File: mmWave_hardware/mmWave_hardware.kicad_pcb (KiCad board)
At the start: 6 copper layers, 49 x 21.6 mm, 48 parts, among them J1 Conn_02x08_Top_Bottom, U1 IWRL6432BDBAAMFR, U2 W25Q128JVS, U3 AMS1117-3.3, U4 TPS628502QDRLRQ1, Y1 40.000

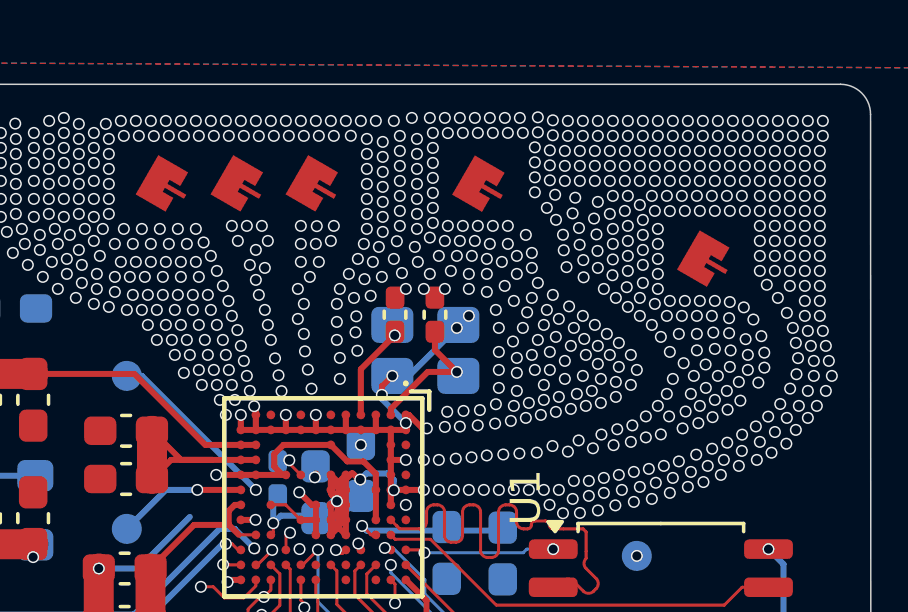
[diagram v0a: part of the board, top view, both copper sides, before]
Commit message: unrouting started
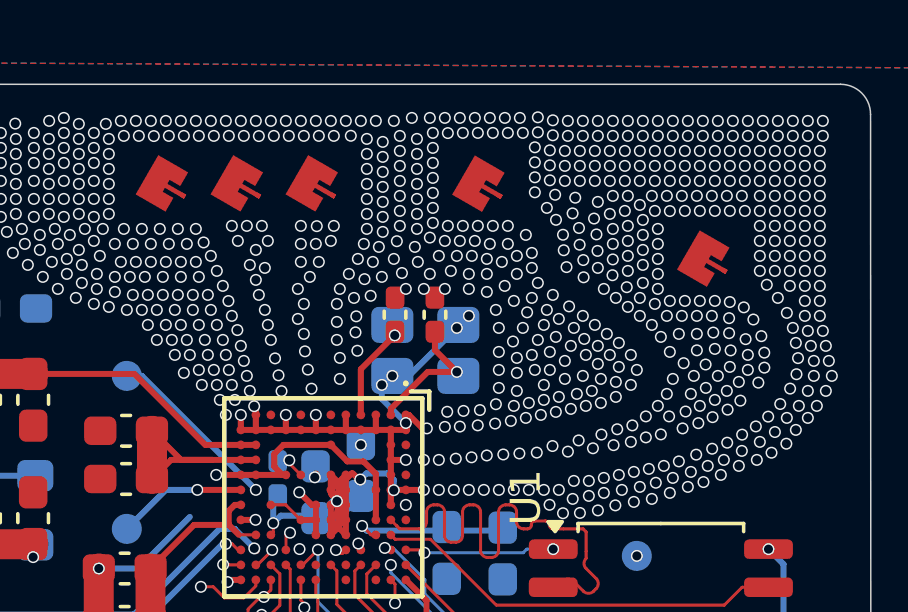
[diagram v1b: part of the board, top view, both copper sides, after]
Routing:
- net UART_RTS: track 42.3 -> 0.88 mm
- net GPIO_5: track 41.8 -> 0.69 mm
- net 1v8: track 78.6 -> 70.7 mm

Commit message: unrouted all
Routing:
- net GND: track 75.7 -> 0.00 mm
- net 1v8: track 70.7 -> 0.00 mm
- net 3v3: track 66.2 -> 0.00 mm
- net RS232_TX: track 52.1 -> 0.00 mm
- net SPI0_CLK: track 51.7 -> 0.00 mm
- net RS232_RX: track 51.0 -> 0.00 mm
- net SPI0_CS0_N: track 48.9 -> 0.00 mm
- net SPI0_MISO: track 45.0 -> 0.00 mm
- net SPI0_MOSI: track 44.9 -> 0.00 mm
- net UART_RX: track 40.4 -> 0.00 mm
- net GPIO_2: track 39.0 -> 0.00 mm
- net UART_TX: track 36.8 -> 0.00 mm
- net NRST_MAIN: track 35.4 -> 0.00 mm
- net VIN: track 23.0 -> 0.00 mm
- net /QSPI_1: track 17.1 -> 0.00 mm
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
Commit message: routing done
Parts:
- moved R3 10.2 mm to (58.5, 61.6)
- moved R6 9.69 mm to (58.5, 64.0)
- moved R2 7.50 mm to (58.5, 62.8)
- moved R4 7.22 mm to (57.9, 71.4)
- moved TP5 6.23 mm to (73.1, 69.3)
- moved C20 6.22 mm to (58.0, 67.2), turned to 90 degrees
- moved R5 5.37 mm to (57.9, 73.1)
- moved TP4 1.82 mm to (73.2, 66.4)
- moved R7 1.00 mm to (60.6, 67.5)
- moved C21 0.88 mm to (62.1, 70.7), turned to -90 degrees
- moved C18 0.43 mm to (64.6, 72.8)
- moved C9 0.14 mm to (76.5, 73.5)
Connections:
- J1 pad 10: SPI0_CS0_N -> UART_RTS
- J1 pad 11: SPI0_MISO -> UART_RX
- J1 pad 12: SPI0_MOSI -> UART_TX
- J1 pad 13: RS232_TX -> SPI0_CS0_N
- J1 pad 14: RS232_RX -> SPI0_CLK
- J1 pad 15: NRST_MAIN -> SPI0_MOSI
- J1 pad 16: VIN -> SPI0_MISO
- J1 pad 2: GPIO_2 -> VIN
- J1 pad 3: GND -> GPIO_2
- J1 pad 5: GND -> RS232_RX
- J1 pad 6: UART_RTS -> RS232_TX
- J1 pad 7: UART_RX -> unconnected-(J1-Pin_7-Pad7)
- J1 pad 8: UART_TX -> NRST_MAIN
- J1 pad 9: SPI0_CLK -> unconnected-(J1-Pin_9-Pad9)
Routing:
- net 3v3: track 0.00 -> 80.6 mm
- net GND: track 0.00 -> 52.3 mm
- net SPI0_CS0_N: track 0.00 -> 42.8 mm
- net 1v8: track 0.00 -> 42.5 mm, vias 6 -> 5
- net RS232_RX: track 0.00 -> 38.9 mm
- net SPI0_CLK: track 0.00 -> 38.0 mm
- net VIN: track 0.00 -> 35.1 mm, vias 3 -> 1
- net RS232_TX: track 0.00 -> 35.0 mm, vias 2 -> 1
- net SPI0_MOSI: track 0.00 -> 33.7 mm
- net SPI0_MISO: track 0.00 -> 33.7 mm
- net GPIO_2: track 0.00 -> 31.7 mm
- net UART_RX: track 0.00 -> 30.3 mm
- net UART_TX: track 0.00 -> 30.1 mm
- net NRST_MAIN: track 0.00 -> 29.6 mm
- net GPIO_5: track 0.00 -> 29.1 mm
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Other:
- board text removed: "ABCS"
- board text removed: "If you can see this, You have voided your warranty"

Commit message: Final PCB(Probably)
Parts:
- moved C10 78.1 mm to (144.8, 109.8)
- moved C11 78.1 mm to (141.4, 107.4)
- moved C12 78.1 mm to (141.4, 109.2)
- moved C13 78.1 mm to (136.7, 105.7)
- moved C14 78.1 mm to (138.3, 105.7)
- moved C17 78.1 mm to (149.2, 104.1)
- moved C18 78.1 mm to (132.9, 110.7)
- moved C19 78.1 mm to (129.6, 99.5)
- moved C2 78.1 mm to (151.7, 99.0)
- moved C20 78.1 mm to (126.3, 105.1)
- moved C21 78.1 mm to (130.3, 108.5)
- moved C22 78.1 mm to (136.3, 105.2)
- moved C23 78.1 mm to (137.6, 98.7)
- moved C24 78.1 mm to (133.9, 101.7)
- moved C3 78.1 mm to (152.1, 106.9)
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
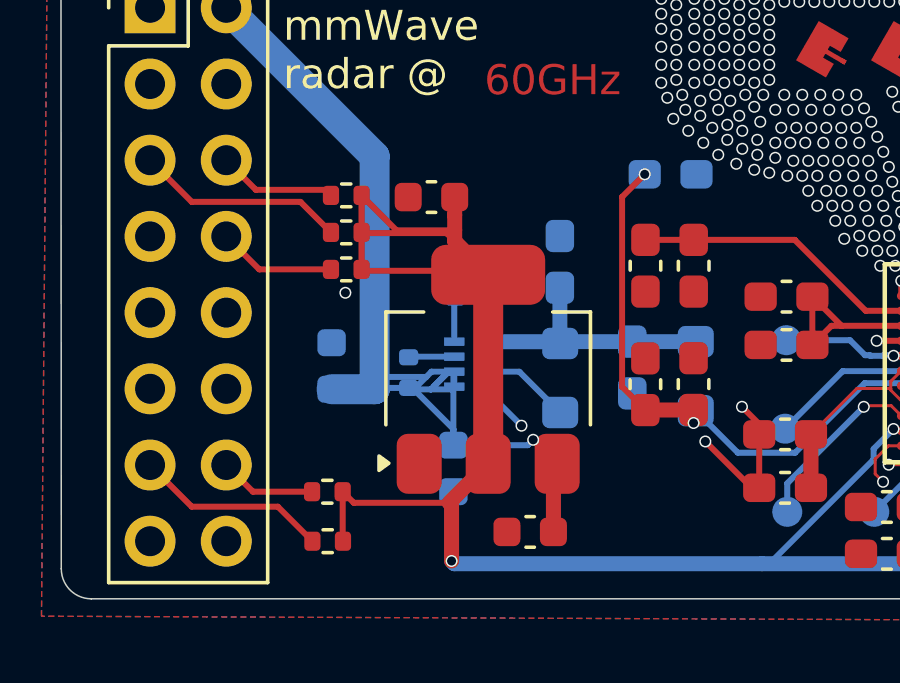
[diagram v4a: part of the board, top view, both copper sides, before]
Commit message: fixed footprint issue
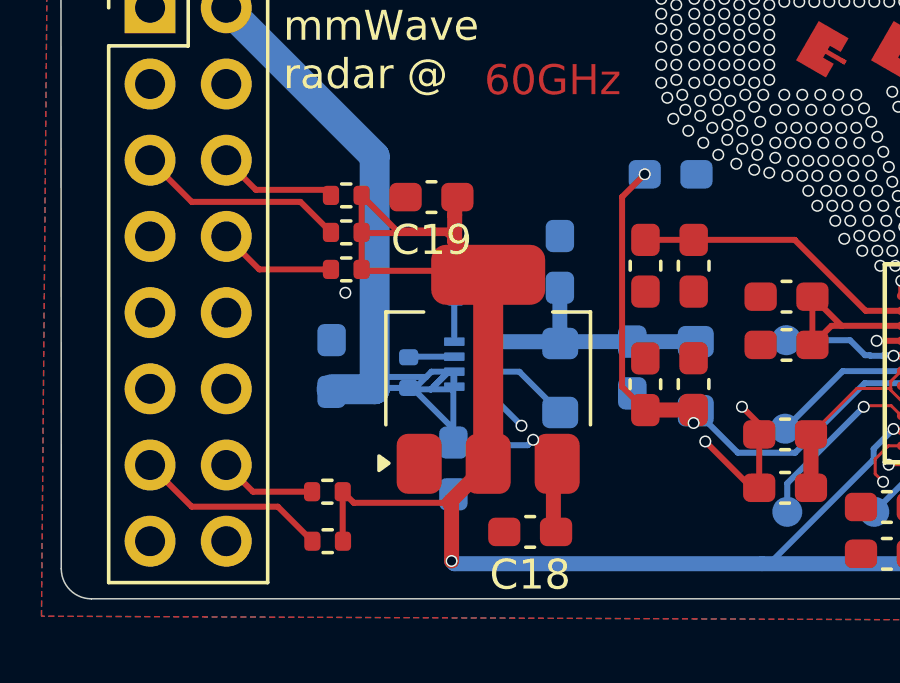
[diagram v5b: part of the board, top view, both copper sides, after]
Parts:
- C18, C19, C20, C21: footprint Capacitor_SMD:C_0603_1608Metric -> Capacitor_SMD:C_0603_1608Metric_Pad1.08x0.95mm_HandSolder

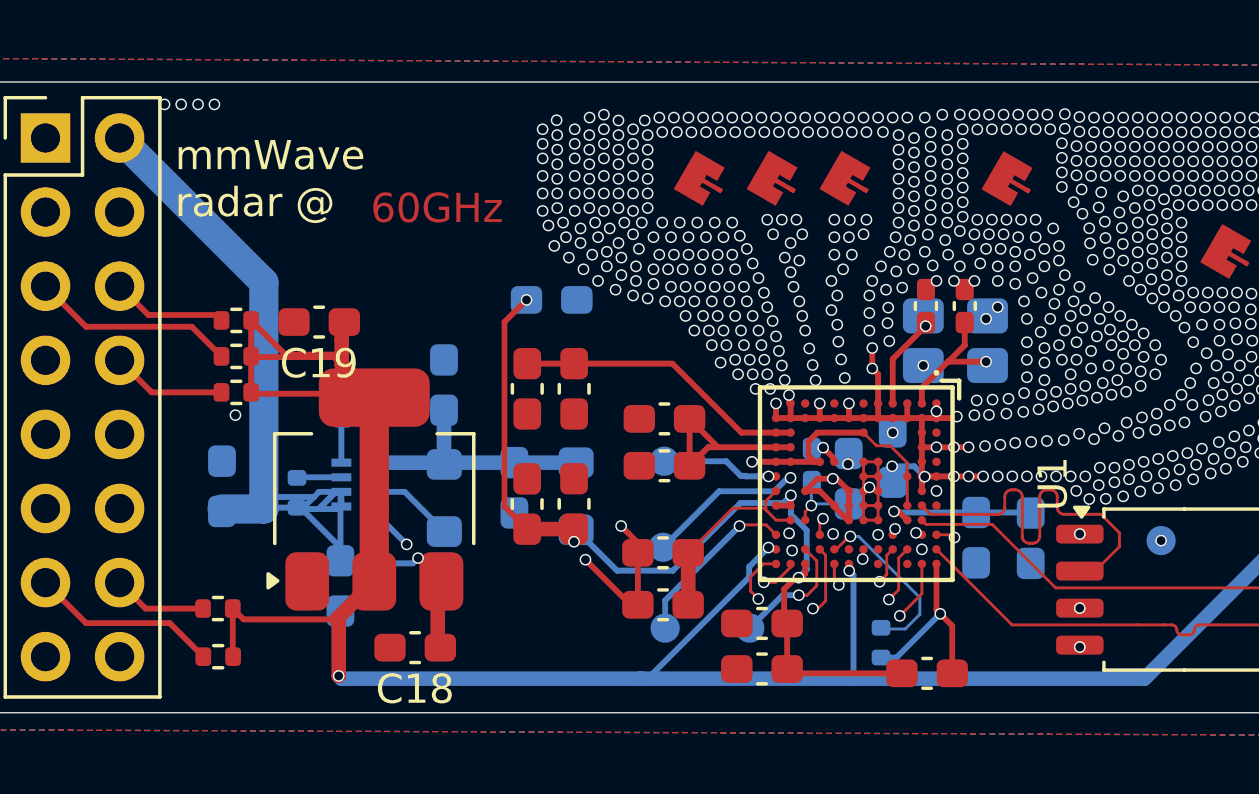
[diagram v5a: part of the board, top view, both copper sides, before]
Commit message: changed silkscreen
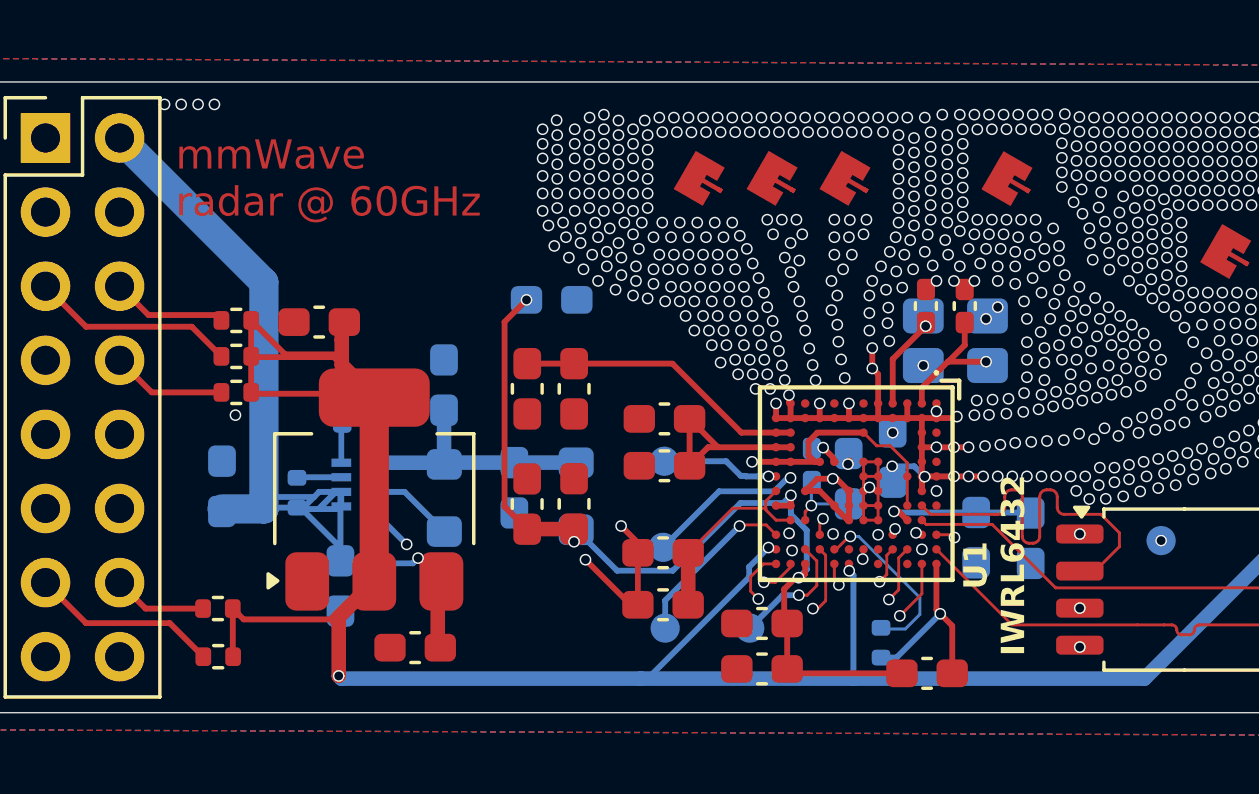
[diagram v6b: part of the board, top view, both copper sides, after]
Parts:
- R8: footprint Resistor_SMD:R_0402_1005Metric -> Resistor_SMD:R_0402_1005Metric_Pad0.72x0.64mm_HandSolder
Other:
- board text added: "U1 IWRL6432"
- board text added: "mmWave radar @ 60GHz"
- board text removed: "60GHz"
- board text removed: "mmWave radar @"
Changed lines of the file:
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@@
 		(at 147.997655 105.041 -90)
 		(property "Reference" "U1"
-			(at 0 -6.75 90)
+			(at 2.479 -4.322345 90)
 			(layer "F.SilkS")
+			(hide yes)
 			(effects
 				(font
@@
 			(at 0 -1.43 180)
 			(layer "F.SilkS")
+			(hide yes)
 			(effects
 				(font
@@
 			(at 0 -1.43 180)
 			(layer "F.SilkS")
+			(hide yes)
 			(effects
 				(font
@@
 		(embedded_fonts no)
 	)
-	(footprint "Resistor_SMD:R_0402_1005Metric"
+	(footprint "Resistor_SMD:R_0402_1005Metric_Pad0.72x0.64mm_HandSolder"
 		(layer "B.Cu")
 		(at 130.380155 102.341 90)
-		(descr "Resistor SMD 0402 (1005 Metric), square (rectangular) end terminal, IPC-7351 nominal, (Body size source: IPC-SM-782 page 72, https://www.pcb-3d.com/wordpress/wp-content/uploads/ipc-sm-782a_amendment_1_and_2.pdf), generated with kicad-footprint-generator")
-		(tags "resistor")
+		(descr "Resistor SMD 0402 (1005 Metric), square (rectangular) end terminal, IPC-7351 nominal with elongated pad for handsoldering. (Body size source: IPC-SM-782 page 72, https://www.pcb-3d.com/wordpress/wp-content/uploads/ipc-sm-782a_amendment_1_and_2.pdf), generated with kicad-footprint-generator")
+		(tags "resistor handsolder")
 		(property "Reference" "R8"
-			(at 0 1.17 90)
+			(at 0 1.17 270)
 			(layer "B.SilkS")
-			(hide yes)
 			(effects
 				(font
@@
 		)
 		(property "Value" "18k"
-			(at 0 -1.17 90)
+			(at 0 -1.17 270)
 			(layer "B.Fab")
 			(effects
@@
 		)
 		(property "Datasheet" ""
-			(at 0 0 90)
+			(at 0 0 270)
 			(layer "B.Fab")
 			(hide yes)
@@
 		)
 		(property "Description" "Resistor, small symbol"
-			(at 0 0 90)
+			(at 0 0 270)
 			(layer "B.Fab")
 			(hide yes)
@@
 		(attr smd)
 		(fp_line
-			(start -0.153641 -0.38)
-			(end 0.153641 -0.38)
+			(start -0.167621 -0.38)
+			(end 0.167621 -0.38)
 			(stroke
 				(width 0.12)
@@
 		)
 		(fp_line
-			(start -0.153641 0.38)
-			(end 0.153641 0.38)
+			(start -0.167621 0.38)
+			(end 0.167621 0.38)
 			(stroke
 				(width 0.12)
@@
 		)
 		(fp_line
-			(start 0.93 -0.47)
-			(end -0.93 -0.47)
+			(start 1.11 -0.47)
+			(end -1.11 -0.47)
 			(stroke
 				(width 0.05)
@@
 		)
 		(fp_line
-			(start -0.93 -0.47)
-			(end -0.93 0.47)
+			(start -1.11 -0.47)
+			(end -1.11 0.47)
 			(stroke
 				(width 0.05)
@@
 		)
 		(fp_line
-			(start 0.93 0.47)
-			(end 0.93 -0.47)
+			(start 1.11 0.47)
+			(end 1.11 -0.47)
 			(stroke
 				(width 0.05)
@@
 		)
 		(fp_line
-			(start -0.93 0.47)
-			(end 0.93 0.47)
+			(start -1.11 0.47)
+			(end 1.11 0.47)
 			(stroke
 				(width 0.05)
@@
 		)
 		(fp_text user "${REFERENCE}"
-			(at 0 0 90)
+			(at 0 0 270)
 			(layer "B.Fab")
 			(effects
@@
 		)
 		(pad "1" smd roundrect
-			(at -0.51 0 90)
-			(size 0.54 0.64)
+			(at -0.5975 0 90)
+			(size 0.715 0.64)
 			(layers "B.Cu" "B.Mask" "B.Paste")
 			(roundrect_rratio 0.25)
@@
 		)
 		(pad "2" smd roundrect
-			(at 0.51 0 90)
-			(size 0.54 0.64)
+			(at 0.5975 0 90)
+			(size 0.715 0.64)
 			(layers "B.Cu" "B.Mask" "B.Paste")
 			(roundrect_rratio 0.25)
@@
 			(at 0 1.43 270)
 			(layer "B.SilkS")
+			(hide yes)
 			(effects
 				(font
@@
 			(at 0 1.43 90)
 			(layer "B.SilkS")
+			(hide yes)
 			(effects
 				(font
@@
 		(layer "Edge.Cuts")
 	)
-	(gr_text "60GHz"
-		(at 131.347655 96.191 0)
+	(gr_text "mmWave\nradar @ 60GHz"
+		(at 124.67 95.97 0)
 		(layer "F.Cu")
 		(effects
 			(font
 				(size 1 1)
-				(thickness 0.15)
+				(thickness 0.125)
 			)
 			(justify left bottom)
 		)
 	)
-	(gr_text "60GHz"
-		(at 131.347655 96.191 0)
+	(gr_text "mmWave\nradar @ 60GHz"
+		(at 124.67 95.97 0)
 		(layer "F.Mask")
 		(effects
 			(font
 				(size 1 1)
-				(thickness 0.15)
+				(thickness 0.125)
 			)
 			(justify left bottom)
 		)
 	)
-	(gr_text "mmWave\nradar @"
-		(at 124.647655 95.991 0)
+	(gr_text "U1\nIWRL6432"
+		(at 153.85 107.84 90)
 		(layer "F.SilkS")
 		(effects
 			(font
-				(size 1 1)
-				(thickness 0.15)
+				(size 0.8 0.8)
+				(thickness 0.16)
+				(bold yes)
 			)
-			(justify left bottom)
+			(justify bottom)
 		)
 	)
